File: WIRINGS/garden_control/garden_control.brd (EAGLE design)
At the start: 45.7 x 37.5 mm, 14 parts

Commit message: updated boards and wirings
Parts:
- removed C1, C3: (no value), rcl:C1210
- removed LED1: (no value), led:LED3MM
- removed R1, R2, R3, R4, R5: 10k, rcl:R0805
- added JP10, JP8: (no value), pinhead:1X06
- added JP11, JP9: (no value), pinhead:1X02
- added JP4: (no value), pinhead:1X10
- added JP6: (no value), pinhead:1X08
- JP1: device pinhead:1X04 -> pinhead:1X08
- JP2, JP5: device pinhead:1X03 -> pinhead:1X08
- JP3: device pinhead:1X02 -> pinhead:1X08
- JP7: device pinhead:1X06 -> pinhead:1X02
- moved JP7 71.7 mm to (8.89, -40.6)
- moved JP5 38.6 mm to (16.5, -10.2), turned to 0 degrees
- moved U$2 16.6 mm to (11.3, 0.64)
- moved JP2 14.8 mm to (10.2, 40.0), turned to 270 degrees
- moved JP1 13.4 mm to (35.6, 40.0), turned to 90 degrees
- moved JP3 4.49 mm to (23.5, 5.08), turned to 0 degrees
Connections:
- net NA renamed GPA1
- removed net N$2: LED1.A, R3.2
- removed net P0: JP7.6
- removed net P1: JP7.5
- removed net P2: JP1.3, JP7.4, R2.2
- removed net P3: JP2.1, JP7.3, R3.1
- removed net P4: JP7.2, R4.2, R5.1
- removed net P5: JP7.1, R1.1
- removed net VIN: C3.1, JP3.1, JP5.1, R4.1
- new net +3V3: JP3.1, JP4.1, JP4.2, JP4.3, JP4.4
- new net GPA0: JP1.1
- new net GPA2: JP1.3
- new net GPA3: JP1.4
- new net GPA4: JP1.5
- new net GPA5: JP1.6
- new net GPA6: JP1.7
- new net GPA7: JP1.8
- new net GPB0: JP2.1
- new net GPB1: JP2.2
- new net GPB2: JP2.3
- new net GPB3: JP2.4
- new net GPB4: JP2.5
- new net GPB5: JP2.6
- new net GPB6: JP2.7
- new net GPB7: JP2.8
- new net INTA: JP3.8
- new net INTB: JP3.7
- new net NRES: JP3.6
- new net R1_GND: JP8.6
- new net R1_J_VCC: JP9.1
- new net R1_R1: JP8.2
- new net R1_R2: JP8.3
- new net R1_R3: JP8.4
- new net R1_R4: JP8.5
- new net R1_VCC: JP8.1, JP9.2
- new net R2_GND: JP10.6
- new net R2_J_VCC: JP11.1
- new net R2_R1: JP10.2
- new net R2_R2: JP10.3
- new net R2_R3: JP10.4
- new net R2_R4: JP10.5
- new net R2_VCC: JP10.1, JP11.2
- new net SCA: JP3.4
- new net SCL: JP3.3
- new net W_3_3V: JP5.1
- new net W_5V: JP6.1
- new net W_A0: JP5.7
- new net W_D0: JP5.6
- new net W_D1_SCL: JP6.6
- new net W_D2_SDA: JP6.5
- new net W_D3: JP6.4
- new net W_D4: JP6.3
- new net W_D5: JP5.5
- new net W_D6: JP5.4
- new net W_D7: JP5.3
- new net W_D8: JP5.2
- new net W_GND: JP6.2
- new net W_RESET: JP5.8
- new net W_RX: JP6.7
- new net W_TX: JP6.8
- net +5V: now also JP4.5, JP4.6, JP4.7; no longer C1.1, JP1.4, JP2.2, JP5.3, R1.2, R2.1
- net DGND: now also JP3.5, JP4.10, JP4.8, JP4.9; no longer C1.2, C3.2, JP1.1, JP2.3, JP5.2, LED1.K, R5.2
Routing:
- net +5V: track 96.6 -> 5.08 mm
- net +3V3: track 0.00 -> 69.1 mm
- net VIN: track 46.7 -> 0.00 mm
- net P3: track 35.5 -> 0.00 mm, vias 2 -> 0
- net INTA: track 0.00 -> 31.9 mm
- net INTB: track 0.00 -> 30.2 mm
- net NRES: track 0.00 -> 26.8 mm
- net DGND: track 24.3 -> 0.00 mm, vias 4 -> 0
- net SCL: track 0.00 -> 19.3 mm
- net P4: track 19.2 -> 0.00 mm
- net SCA: track 0.00 -> 16.2 mm
- net P2: track 14.5 -> 0.00 mm
- net P5: track 8.50 -> 0.00 mm
- net N$2: track 3.31 -> 0.00 mm
- net P1: track 3.04 -> 0.00 mm, vias 1 -> 0
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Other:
- board size 45.7 x 37.5 mm -> 45.7 x 62.2 mm
- board text added: "PN39022R1B1"
- board text added: "WSHIELD_MCP_BASIC"
- board text removed: "PN39023R1B0"
- board text removed: "WSHIELD_ATTINY_ BATSENSE2"

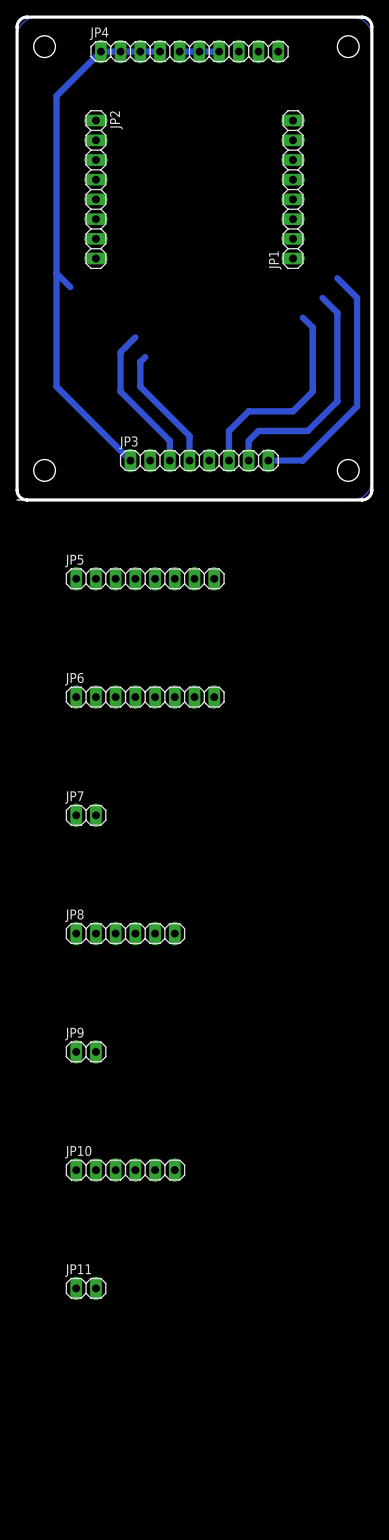
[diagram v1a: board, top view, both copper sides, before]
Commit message: updated wiring
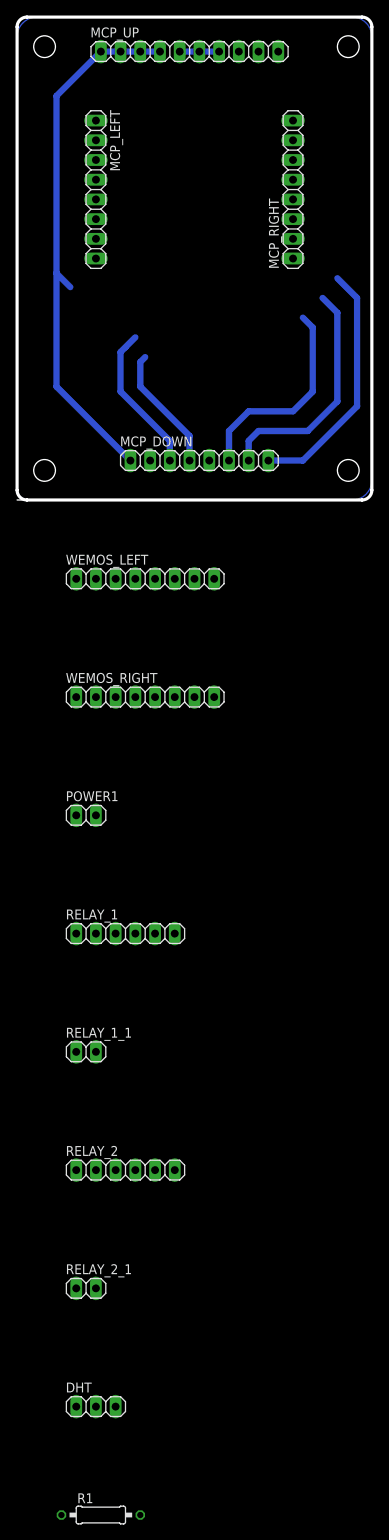
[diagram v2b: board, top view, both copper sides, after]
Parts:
- added DHT: (no value), pinhead:1X03
- added R1: 10k, rcl:0207/10
- renumbered JP1 to MCP_RIGHT, JP10 to RELAY_2, JP11 to RELAY_2_1, JP2 to MCP_LEFT, JP3 to MCP_DOWN, JP4 to MCP_UP, JP5 to WEMOS_LEFT, JP6 to WEMOS_RIGHT, JP7 to POWER1, JP8 to RELAY_1, JP9 to RELAY_1_1
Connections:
- new net DHT_DATA: DHT.2
- new net DHT_GND: DHT.3
- new net DHT_VCC: DHT.1
- new net GND_1: POWER1.2
- new net N$4: R1.2
- new net N$5: R1.1
- new net POWER_5V_1: POWER1.1
